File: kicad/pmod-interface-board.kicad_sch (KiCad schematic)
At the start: 11 parts, among them J1 PMOD Connector 1, J2 PMOD Connector 2, J3 GB Cart Breakout, U1 74HCT541, U2 74HCT541, U3 74HC595, U4 74HC595, U5 74HC595, U6 74HC597

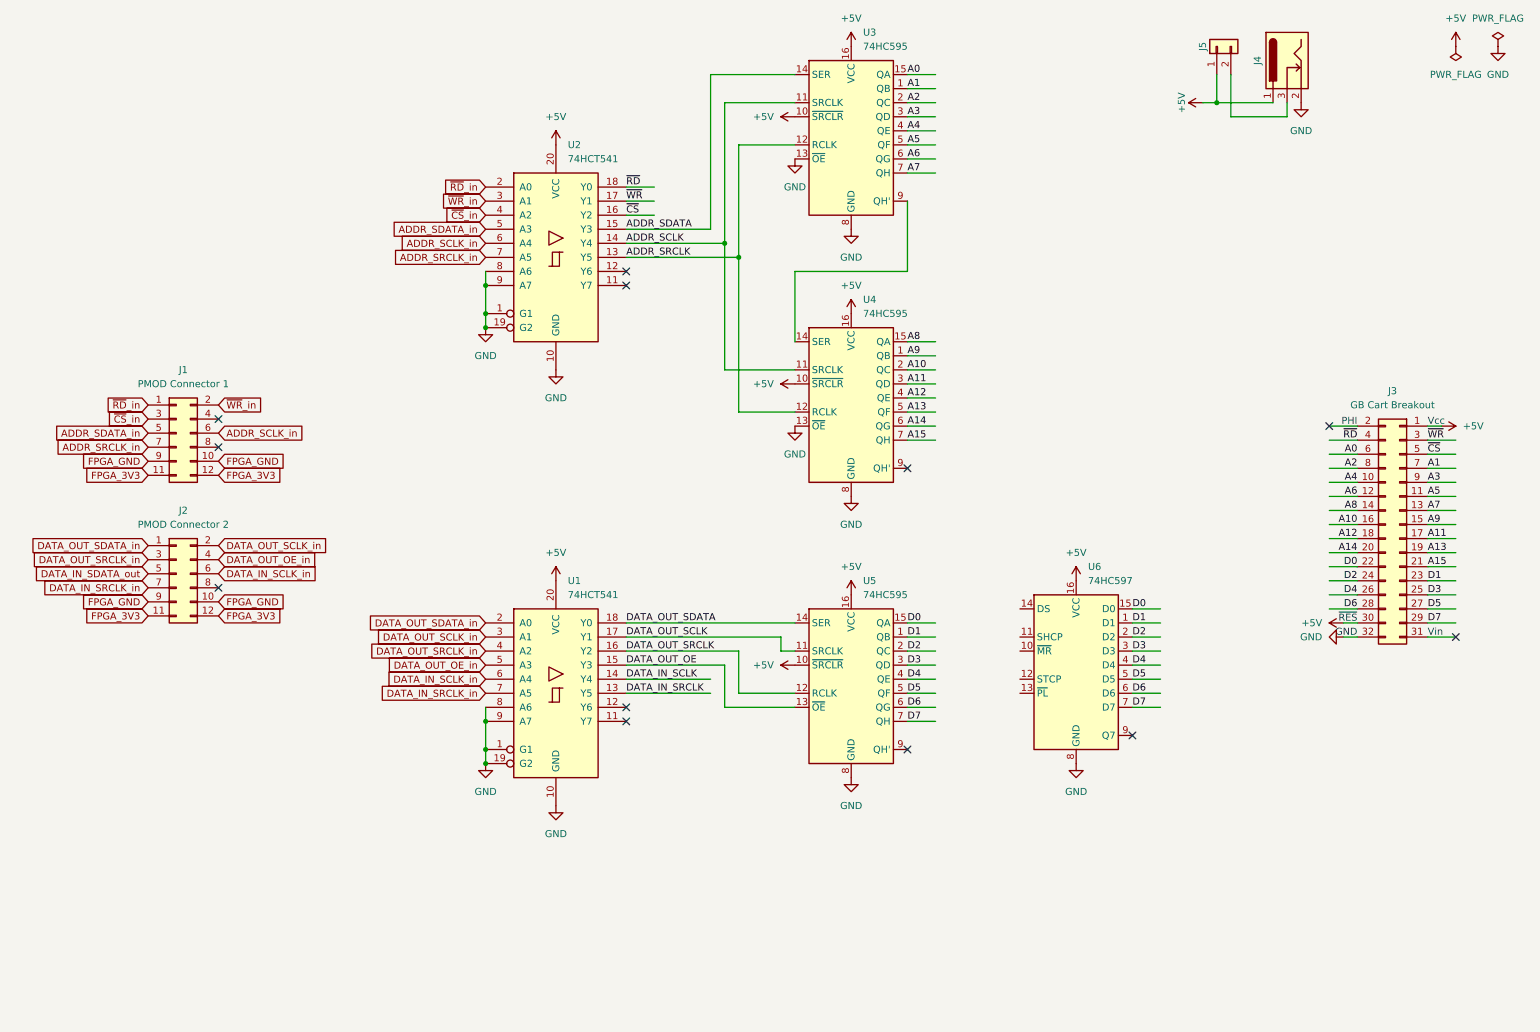
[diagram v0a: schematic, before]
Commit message: kicad: finished interface board schematics
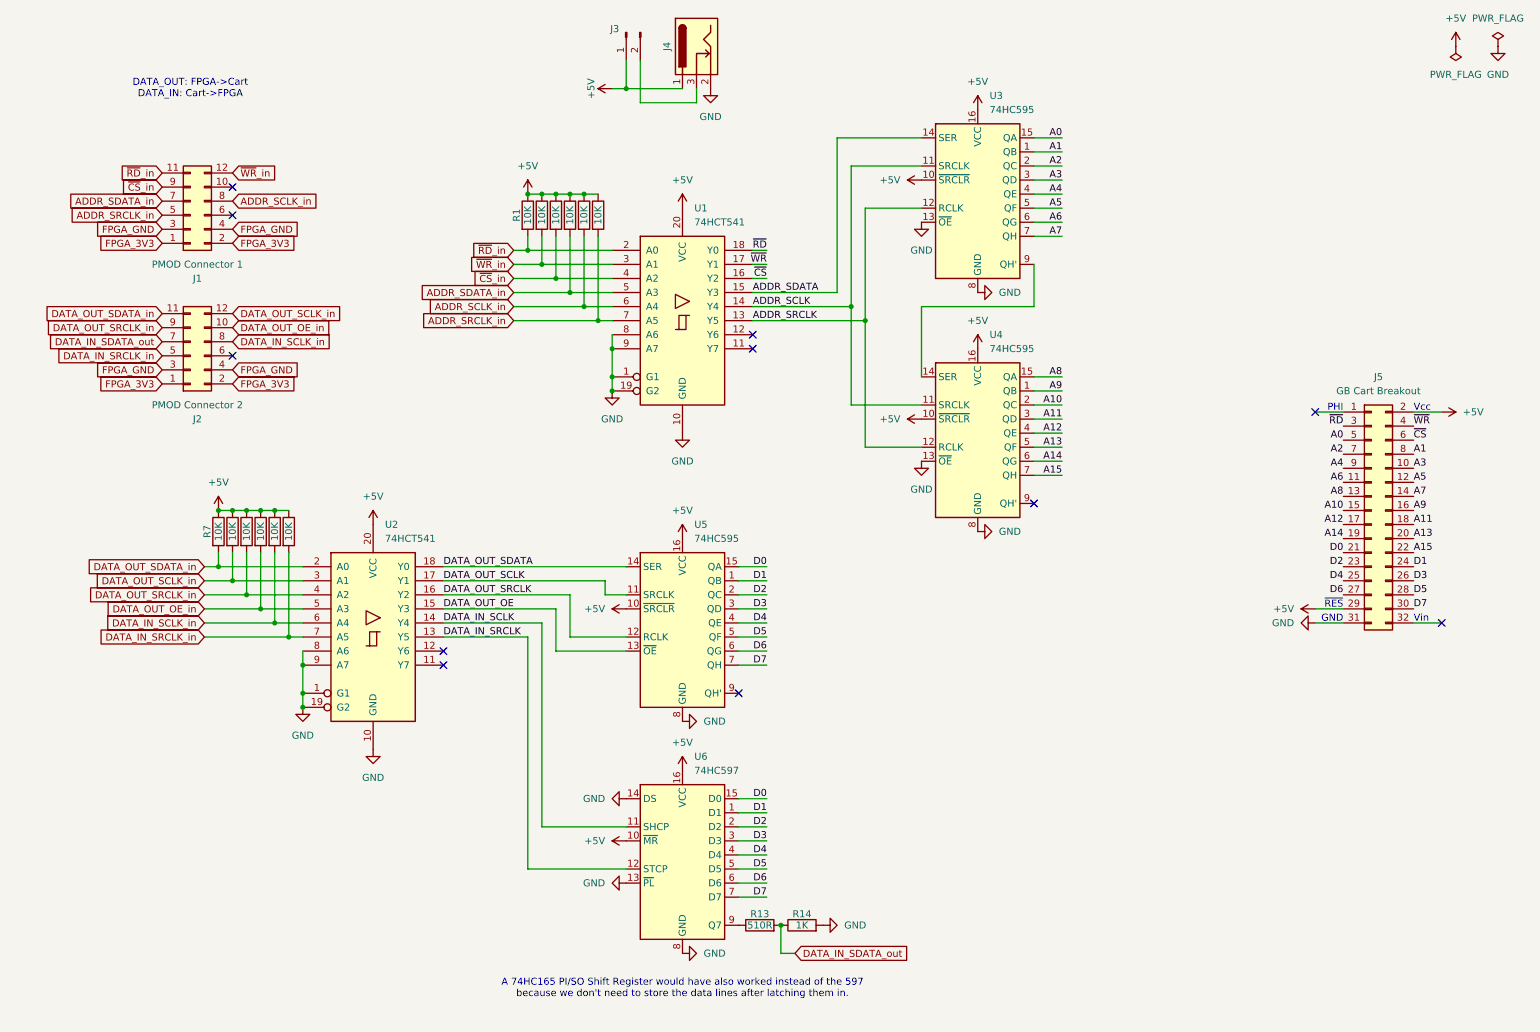
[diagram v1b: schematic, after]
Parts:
- removed J5: ~, Connector_PinHeader_2.54mm:PinHeader_1x02_P2.54mm_Horizontal, symbol Connector_Generic:Conn_01x02
- added J3: ~, Connector_PinHeader_2.54mm:PinHeader_1x02_P2.54mm_Horizontal, symbol Connector:Conn_01x02_Pin
- added R1, R10, R11, R12, R2, R3, R4, R5, R6, R7, R8, R9: 10K, Resistor_THT:R_Axial_DIN0207_L6.3mm_D2.5mm_P7.62mm_Horizontal, symbol Device:R
- added R13: 510R, Resistor_THT:R_Axial_DIN0207_L6.3mm_D2.5mm_P7.62mm_Horizontal, symbol Device:R
- added R14: 1K, Resistor_THT:R_Axial_DIN0207_L6.3mm_D2.5mm_P7.62mm_Horizontal, symbol Device:R
- J1, J2: footprint (none) -> Connector_PinHeader_2.54mm:PinHeader_2x06_P2.54mm_Horizontal
- J5: renamed from J3; footprint (none) -> Connector_PinHeader_2.54mm:PinHeader_2x16_P2.54mm_Vertical
- U1: renamed from U2; footprint (none) -> Package_DIP:DIP-20_W7.62mm
- U2: renamed from U1; footprint (none) -> Package_DIP:DIP-20_W7.62mm
- U3, U4, U5, U6: footprint (none) -> Package_DIP:DIP-16_W7.62mm
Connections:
- net +5V: now also J5.2 (Pin_2), J5.29 (Pin_29), U6.10 (~{MR}), J3.1 (Pin_1), R1.1, R10.1, R11.1, R12.1, R2.1, R3.1, R4.1, R5.1, R6.1, R7.1, R8.1, R9.1; no longer J5.1 (Pin_1), J5.30 (Pin_30)
- net A0: now also J5.5 (Pin_5); no longer J5.6 (Pin_6)
- net A1: now also J5.8 (Pin_8); no longer J5.7 (Pin_7)
- net A10: now also J5.15 (Pin_15); no longer J5.16 (Pin_16)
- net A11: now also J5.18 (Pin_18); no longer J5.17 (Pin_17)
- net A12: now also J5.17 (Pin_17); no longer J5.18 (Pin_18)
- net A13: now also J5.20 (Pin_20); no longer J5.19 (Pin_19)
- net A14: now also J5.19 (Pin_19); no longer J5.20 (Pin_20)
- net A15: now also J5.22 (Pin_22); no longer J5.21 (Pin_21)
- net A2: now also J5.7 (Pin_7); no longer J5.8 (Pin_8)
- net A3: now also J5.10 (Pin_10); no longer J5.9 (Pin_9)
- net A4: now also J5.9 (Pin_9); no longer J5.10 (Pin_10)
- net A5: now also J5.12 (Pin_12); no longer J5.11 (Pin_11)
- net A6: now also J5.11 (Pin_11); no longer J5.12 (Pin_12)
- net A7: now also J5.14 (Pin_14); no longer J5.13 (Pin_13)
- net A8: now also J5.13 (Pin_13); no longer J5.14 (Pin_14)
- net A9: now also J5.16 (Pin_16); no longer J5.15 (Pin_15)
- net ADDR_SCLK_in: now also J1.8 (Pin_8), R5.2; no longer J1.6 (Pin_6)
- net ADDR_SDATA_in: now also J1.7 (Pin_7), R4.2; no longer J1.5 (Pin_5)
- net ADDR_SRCLK_in: now also J1.5 (Pin_5), R6.2; no longer J1.7 (Pin_7)
- net D0: now also J5.21 (Pin_21); no longer J5.22 (Pin_22)
- net D1: now also J5.24 (Pin_24); no longer J5.23 (Pin_23)
- net D2: now also J5.23 (Pin_23); no longer J5.24 (Pin_24)
- net D3: now also J5.26 (Pin_26); no longer J5.25 (Pin_25)
- net D4: now also J5.25 (Pin_25); no longer J5.26 (Pin_26)
- net D5: now also J5.28 (Pin_28); no longer J5.27 (Pin_27)
- net D6: now also J5.27 (Pin_27); no longer J5.28 (Pin_28)
- net D7: now also J5.30 (Pin_30); no longer J5.29 (Pin_29)
- net DATA_IN_SCLK: now also U6.11 (SHCP)
- net DATA_IN_SCLK_in: now also J2.8 (Pin_8), R11.2; no longer J2.6 (Pin_6)
- net DATA_IN_SDATA_out: now also J2.7 (Pin_7), R13.2, R14.1; no longer J2.5 (Pin_5)
- net DATA_IN_SRCLK: now also U6.12 (STCP)
- net DATA_IN_SRCLK_in: now also J2.5 (Pin_5), R12.2; no longer J2.7 (Pin_7)
- net DATA_OUT_OE_in: now also J2.10 (Pin_10), R10.2; no longer J2.4 (Pin_4)
- net DATA_OUT_SCLK_in: now also J2.12 (Pin_12), R8.2; no longer J2.2 (Pin_2)
- net DATA_OUT_SDATA_in: now also J2.11 (Pin_11), R7.2; no longer J2.1 (Pin_1)
- net DATA_OUT_SRCLK_in: now also J2.9 (Pin_9), R9.2; no longer J2.3 (Pin_3)
- net FPGA_3V3: now also J1.1 (Pin_1), J1.2 (Pin_2), J2.1 (Pin_1), J2.2 (Pin_2); no longer J1.11 (Pin_11), J1.12 (Pin_12), J2.11 (Pin_11), J2.12 (Pin_12)
- net FPGA_GND: now also J1.3 (Pin_3), J1.4 (Pin_4), J2.3 (Pin_3), J2.4 (Pin_4); no longer J1.10 (Pin_10), J1.9 (Pin_9), J2.10 (Pin_10), J2.9 (Pin_9)
- net GND: now also J5.31 (Pin_31), U6.13 (~{PL}), U6.14 (DS), R14.2; no longer J5.32 (Pin_32)
- net ~{CS}: now also J5.6 (Pin_6); no longer J5.5 (Pin_5)
- net ~{CS}_in: now also J1.9 (Pin_9), R3.2; no longer J1.3 (Pin_3)
- net ~{RD}: now also J5.3 (Pin_3); no longer J5.4 (Pin_4)
- net ~{RD}_in: now also J1.11 (Pin_11), R1.2; no longer J1.1 (Pin_1)
- net ~{WR}: now also J5.4 (Pin_4); no longer J5.3 (Pin_3)
- net ~{WR}_in: now also J1.12 (Pin_12), R2.2; no longer J1.2 (Pin_2)
- net at J4.3: now also J3.2 (Pin_2)
- net at U6.9 (Q7): now also R13.1
- no-connect marks 12 -> 11
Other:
- note added: "A 74HC165 PI/SO Shift Register would have also worked instead of the 597 because we don't need to store the data lines after latching them in."
- note added: "DATA_OUT: FPGA->Cart DATA_IN: Cart->FPGA"
- moved on the sheet: J1, J2, J4, J5, U1, U2, U3, U4, U5, U6

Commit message: kicad: added decoupling caps
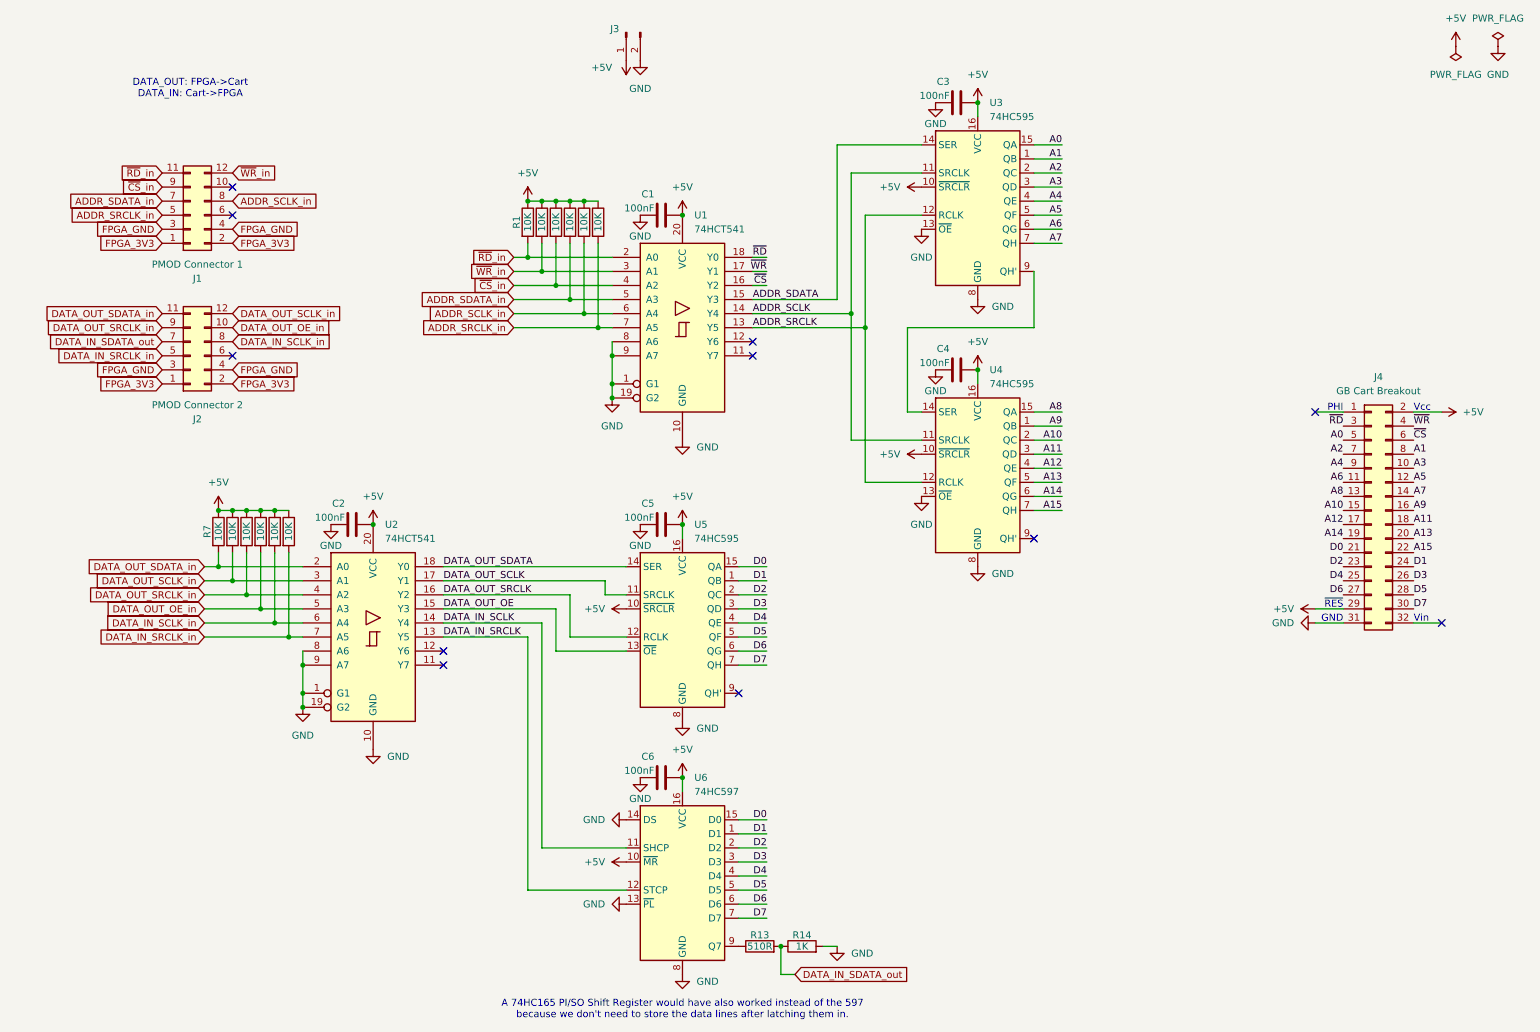
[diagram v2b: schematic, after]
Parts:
- removed J4: ~, Connector_BarrelJack:BarrelJack_Horizontal, symbol Connector:Barrel_Jack_Switch
- added C1, C2, C3, C4, C5, C6: 100nF, Capacitor_THT:C_Disc_D4.7mm_W2.5mm_P5.00mm, symbol Device:C
- renumbered J5 to J4
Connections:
- net +5V: now also C1.1, C2.1, C3.1, C4.1, C5.1, C6.1
- net GND: now also J3.2 (Pin_2), C1.2, C2.2, C3.2, C4.2, C5.2, C6.2
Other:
- moved on the sheet: R1, R13, R14, U1, U3, U4, U6

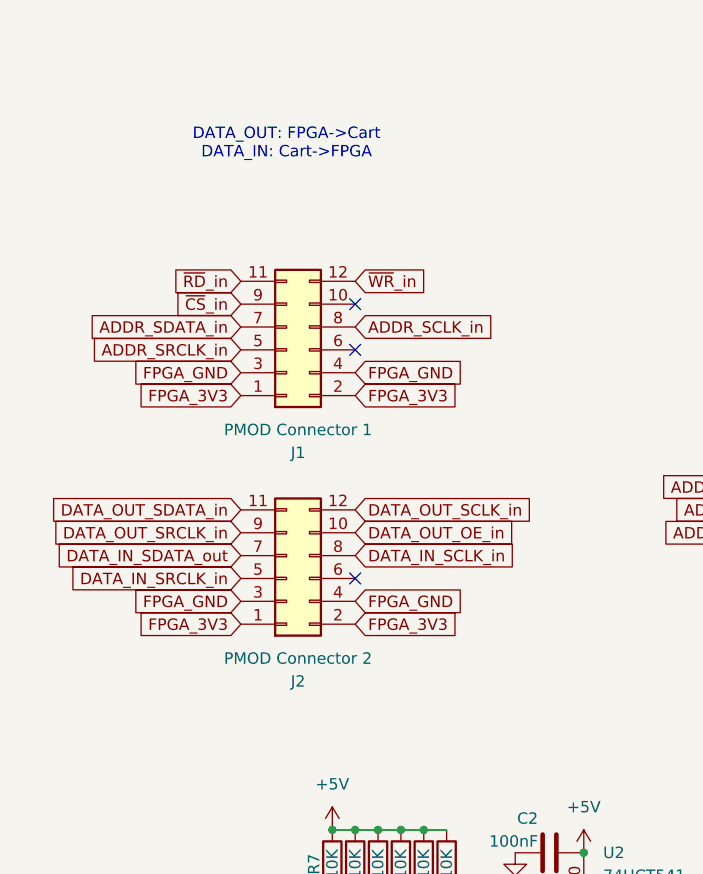
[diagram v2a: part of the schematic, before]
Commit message: kicad: changed schematics pmod gnd/3v3 labeling
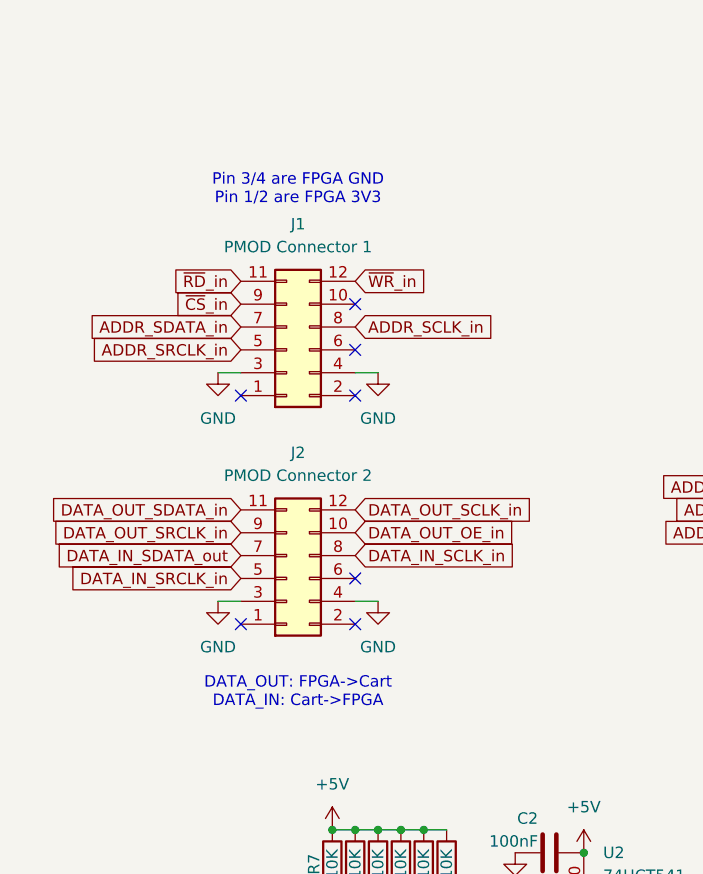
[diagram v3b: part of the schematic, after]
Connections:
- net FPGA_GND is gone; now on net GND: J1.3 (Pin_3), J1.4 (Pin_4), J2.3 (Pin_3), J2.4 (Pin_4)
- removed net FPGA_3V3: J1.1 (Pin_1), J1.2 (Pin_2), J2.1 (Pin_1), J2.2 (Pin_2)
- no-connect marks 11 -> 15
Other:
- note added: "Pin 3/4 are FPGA GND Pin 1/2 are FPGA 3V3"
